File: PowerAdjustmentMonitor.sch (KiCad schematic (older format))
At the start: 0 parts

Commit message: Added Power Control Monitoring Module Schematic
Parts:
- added JP? (x3): JUMPER, ~, symbol JUMPER
- added R? (x8): R, ~, symbol R
- added R? (x2): RVAR, ~, symbol RVAR
- added U? (x2): LM317, ~, symbol LM317
- added U? (x2): 7805, ~, symbol 7805
- added U? (x2): LM324, symbol LM324
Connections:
- new net: R?.1, R?.2, U?.2 (ADJ)
- new net: R?.2, R?.2, U?.2 (ADJ)
- new net +12V: JP?.1, U?.1 (IN), U?.4 (V+), U?.4 (V+), U?.VI
- new net -12V: JP?.1, U?.1 (IN), U?.11 (V-), U?.11 (V-), U?.VI
- new net AGND: JP?.1
- new net FE_V+: JP?.2, U?.VO
- new net FE_V-: JP?.2, U?.VO
- new net GND: JP?.2, R?.1, R?.1, R?.1, R?.2, U?.GND, U?.GND
- new net V+CURR_MON: U?.1, U?.2 (-)
- new net V+_ADJ: R?.2, R?.2
- new net V+_ADJ_MON: R?.1, R?.2
- new net V+_MON: R?.1, R?.1, U?.3 (+), U?.3 (OUT)
- new net V-ADJ_MON: R?.1, R?.2
- new net V-CURR_MON: U?.1, U?.2 (-)
- new net V-_ADJ: R?.1, R?.2
- new net V-_MON: R?.1, R?.2, U?.3 (+), U?.3 (OUT)

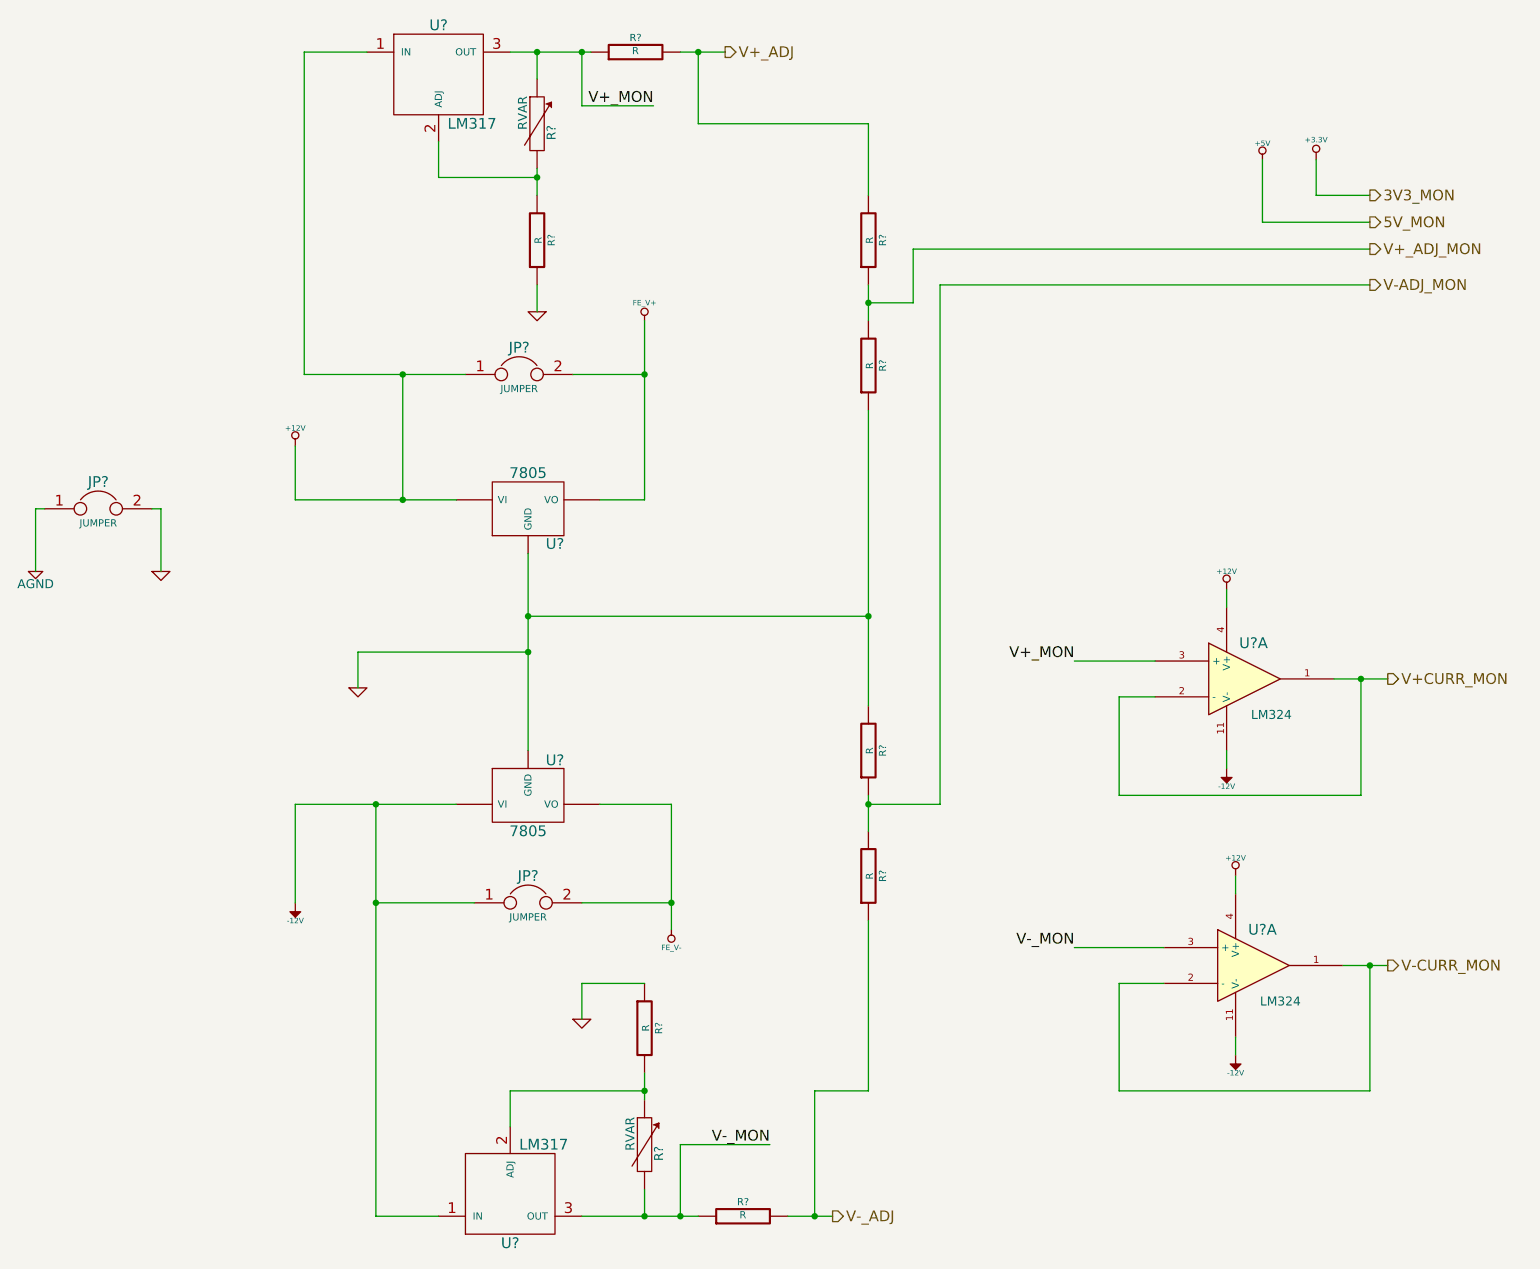
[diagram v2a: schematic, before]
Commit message: Initial Relay PCB Layout
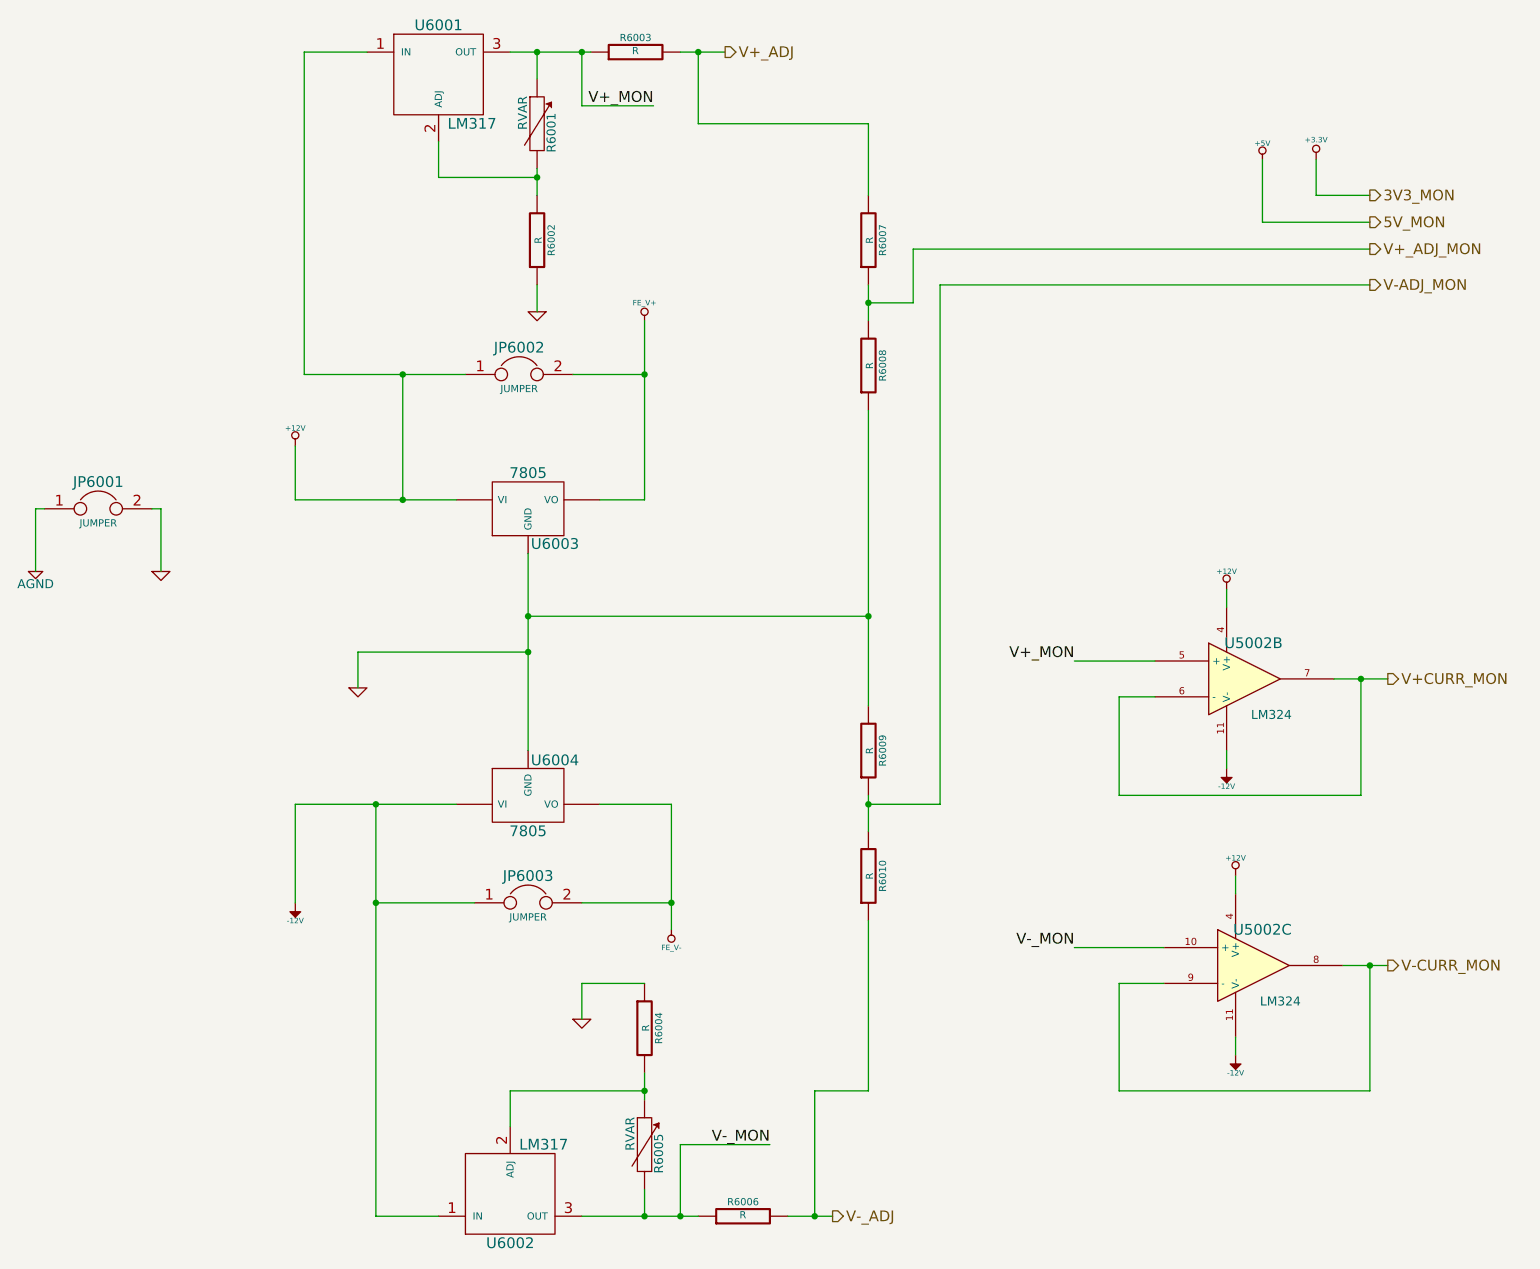
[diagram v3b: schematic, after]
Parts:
- gave numbers to parts that had none: 18
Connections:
- net V+CURR_MON: now also U5002.6 (-), U5002.7; no longer U5002.1, U5002.2 (-)
- net V+_MON: now also U5002.5 (+); no longer U5002.3 (+)
- net V-CURR_MON: now also U5002.8, U5002.9 (-); no longer U5002.1, U5002.2 (-)
- net V-_MON: now also U5002.10 (+); no longer U5002.3 (+)
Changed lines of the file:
@@
 $Descr A4 11693 8268
 encoding utf-8
-Sheet 9 9
+Sheet 6 9
 Title ""
-Date "9 feb 2014"
+Date "17 feb 2014"
 Rev ""
 Comp ""
@@
 $EndDescr
 $Comp
-L +3.3V #PWR?
+L +3.3V #PWR6015
 U 1 1 52F258C0
 P 9300 1600
-F 0 "#PWR?" H 9300 1560 30  0001 C CNN
+F 0 "#PWR6015" H 9300 1560 30  0001 C CNN
 F 1 "+3.3V" H 9300 1710 30  0000 C CNN
 F 2 "" H 9300 1600 60  0000 C CNN
@@
 $EndComp
 $Comp
-L +5V #PWR?
+L +5V #PWR6014
 U 1 1 52F258C6
 P 9000 1600
-F 0 "#PWR?" H 9000 1690 20  0001 C CNN
+F 0 "#PWR6014" H 9000 1690 20  0001 C CNN
 F 1 "+5V" H 9000 1690 30  0000 C CNN
 F 2 "" H 9000 1600 60  0000 C CNN
@@
 $EndComp
 $Comp
-L GND #PWR?
+L GND #PWR6005
 U 1 1 52F2592B
 P 3950 4550
-F 0 "#PWR?" H 3950 4550 30  0001 C CNN
+F 0 "#PWR6005" H 3950 4550 30  0001 C CNN
 F 1 "GND" H 3950 4480 30  0001 C CNN
 F 2 "" H 3950 4550 60  0000 C CNN
@@
 $EndComp
 $Comp
-L -12V #PWR?
+L -12V #PWR6004
 U 1 1 52F25955
 P 3600 5750
-F 0 "#PWR?" H 3600 5880 20  0001 C CNN
+F 0 "#PWR6004" H 3600 5880 20  0001 C CNN
 F 1 "-12V" H 3600 5850 30  0000 C CNN
 F 2 "" H 3600 5750 60  0000 C CNN
@@
 $EndComp
 $Comp
-L +12V #PWR?
+L +12V #PWR6003
 U 1 1 52F25965
 P 3600 3200
-F 0 "#PWR?" H 3600 3150 20  0001 C CNN
+F 0 "#PWR6003" H 3600 3150 20  0001 C CNN
 F 1 "+12V" H 3600 3300 30  0000 C CNN
 F 2 "" H 3600 3200 60  0000 C CNN
@@
 $EndComp
 $Comp
-L LM317 U?
+L LM317 U6002
 U 1 1 52F25974
 P 4800 7350
-F 0 "U?" H 4800 7650 60  0000 C CNN
+F 0 "U6002" H 4800 7650 60  0000 C CNN
 F 1 "LM317" H 4850 7100 60  0000 L CNN
 F 2 "~" H 4800 7350 60  0000 C CNN
@@
 $EndComp
 $Comp
-L JUMPER JP?
+L JUMPER JP6002
 U 1 1 52F259A2
 P 4850 2800
-F 0 "JP?" H 4850 2950 60  0000 C CNN
+F 0 "JP6002" H 4850 2950 60  0000 C CNN
 F 1 "JUMPER" H 4850 2720 40  0000 C CNN
 F 2 "~" H 4850 2800 60  0000 C CNN
@@
 $EndComp
 $Comp
-L JUMPER JP?
+L JUMPER JP6003
 U 1 1 52F259AF
 P 4900 5750
-F 0 "JP?" H 4900 5900 60  0000 C CNN
+F 0 "JP6003" H 4900 5900 60  0000 C CNN
 F 1 "JUMPER" H 4900 5670 40  0000 C CNN
 F 2 "~" H 4900 5750 60  0000 C CNN
@@
 $EndComp
 $Comp
-L AGND #PWR?
+L AGND #PWR6001
 U 1 1 52F25DEE
 P 2150 3900
-F 0 "#PWR?" H 2150 3900 40  0001 C CNN
+F 0 "#PWR6001" H 2150 3900 40  0001 C CNN
 F 1 "AGND" H 2150 3830 50  0000 C CNN
 F 2 "" H 2150 3900 60  0000 C CNN
@@
 $EndComp
 $Comp
-L JUMPER JP?
+L JUMPER JP6001
 U 1 1 52F25DFB
 P 2500 3550
-F 0 "JP?" H 2500 3700 60  0000 C CNN
+F 0 "JP6001" H 2500 3700 60  0000 C CNN
 F 1 "JUMPER" H 2500 3470 40  0000 C CNN
 F 2 "~" H 2500 3550 60  0000 C CNN
@@
 $EndComp
 $Comp
-L GND #PWR?
+L GND #PWR6002
 U 1 1 52F25E16
 P 2850 3900
-F 0 "#PWR?" H 2850 3900 30  0001 C CNN
+F 0 "#PWR6002" H 2850 3900 30  0001 C CNN
 F 1 "GND" H 2850 3830 30  0001 C CNN
 F 2 "" H 2850 3900 60  0000 C CNN
@@
 $EndComp
 $Comp
-L FE_V+ #PWR?
+L FE_V+ #PWR6008
 U 1 1 52F25E8D
 P 5550 2500
-F 0 "#PWR?" H 5550 2600 30  0001 C CNN
+F 0 "#PWR6008" H 5550 2600 30  0001 C CNN
 F 1 "FE_V+" H 5550 2600 30  0000 C CNN
 F 2 "" H 5550 2500 60  0000 C CNN
@@
 $EndComp
 $Comp
-L FE_V- #PWR?
+L FE_V- #PWR6009
 U 1 1 52F25E9C
 P 5700 5900
-F 0 "#PWR?" H 5700 6000 30  0001 C CNN
+F 0 "#PWR6009" H 5700 6000 30  0001 C CNN
 F 1 "FE_V-" H 5700 6000 30  0000 C CNN
 F 2 "" H 5700 5900 60  0000 C CNN
@@
 $EndComp
 $Comp
-L 7805 U?
+L 7805 U6003
 U 1 1 52F25F16
 P 4900 3550
-F 0 "U?" H 5050 3354 60  0000 C CNN
+F 0 "U6003" H 5050 3354 60  0000 C CNN
 F 1 "7805" H 4900 3750 60  0000 C CNN
 F 2 "~" H 4900 3550 60  0000 C CNN
@@
 $EndComp
 $Comp
-L 7805 U?
+L 7805 U6004
 U 1 1 52F25F23
 P 4900 5150
-F 0 "U?" H 5050 4954 60  0000 C CNN
+F 0 "U6004" H 5050 4954 60  0000 C CNN
 F 1 "7805" H 4900 5350 60  0000 C CNN
 F 2 "~" H 4900 5150 60  0000 C CNN
@@
 $EndComp
 $Comp
-L R R?
+L R R6004
 U 1 1 52F25FD8
 P 5550 6450
-F 0 "R?" V 5630 6450 40  0000 C CNN
+F 0 "R6004" V 5630 6450 40  0000 C CNN
 F 1 "R" V 5557 6451 40  0000 C CNN
 F 2 "~" V 5480 6450 30  0000 C CNN
@@
 $EndComp
 $Comp
-L GND #PWR?
+L GND #PWR6007
 U 1 1 52F26054
 P 5200 6400
-F 0 "#PWR?" H 5200 6400 30  0001 C CNN
+F 0 "#PWR6007" H 5200 6400 30  0001 C CNN
 F 1 "GND" H 5200 6330 30  0001 C CNN
 F 2 "" H 5200 6400 60  0000 C CNN
@@
 $EndComp
 $Comp
-L LM317 U?
+L LM317 U6001
 U 1 1 52F26114
 P 4400 1150
-F 0 "U?" H 4400 1450 60  0000 C CNN
+F 0 "U6001" H 4400 1450 60  0000 C CNN
 F 1 "LM317" H 4450 900 60  0000 L CNN
 F 2 "~" H 4400 1150 60  0000 C CNN
@@
 $EndComp
 $Comp
-L R R?
+L R R6002
 U 1 1 52F26120
 P 4950 2050
-F 0 "R?" V 5030 2050 40  0000 C CNN
+F 0 "R6002" V 5030 2050 40  0000 C CNN
 F 1 "R" V 4957 2051 40  0000 C CNN
 F 2 "~" V 4880 2050 30  0000 C CNN
@@
 $EndComp
 $Comp
-L GND #PWR?
+L GND #PWR6006
 U 1 1 52F2612C
 P 4950 2450
-F 0 "#PWR?" H 4950 2450 30  0001 C CNN
+F 0 "#PWR6006" H 4950 2450 30  0001 C CNN
 F 1 "GND" H 4950 2380 30  0001 C CNN
 F 2 "" H 4950 2450 60  0000 C CNN
@@
 V-CURR_MON
 $Comp
-L R R?
+L R R6007
 U 1 1 52F261D2
 P 6800 2050
-F 0 "R?" V 6880 2050 40  0000 C CNN
+F 0 "R6007" V 6880 2050 40  0000 C CNN
 F 1 "R" V 6807 2051 40  0000 C CNN
 F 2 "~" V 6730 2050 30  0000 C CNN
@@
 $EndComp
 $Comp
-L R R?
+L R R6008
 U 1 1 52F261D8
 P 6800 2750
-F 0 "R?" V 6880 2750 40  0000 C CNN
+F 0 "R6008" V 6880 2750 40  0000 C CNN
 F 1 "R" V 6807 2751 40  0000 C CNN
 F 2 "~" V 6730 2750 30  0000 C CNN
@@
 $EndComp
 $Comp
-L R R?
+L R R6009
 U 1 1 52F261DE
 P 6800 4900
-F 0 "R?" V 6880 4900 40  0000 C CNN
+F 0 "R6009" V 6880 4900 40  0000 C CNN
 F 1 "R" V 6807 4901 40  0000 C CNN
 F 2 "~" V 6730 4900 30  0000 C CNN
@@
 $EndComp
 $Comp
-L R R?
+L R R6010
 U 1 1 52F261E4
 P 6800 5600
-F 0 "R?" V 6880 5600 40  0000 C CNN
+F 0 "R6010" V 6880 5600 40  0000 C CNN
 F 1 "R" V 6807 5601 40  0000 C CNN
 F 2 "~" V 6730 5600 30  0000 C CNN
@@
 	9000 1950 9600 1950
 $Comp
-L R R?
+L R R6006
 U 1 1 52F2653F
 P 6100 7500
-F 0 "R?" V 6180 7500 40  0000 C CNN
+F 0 "R6006" V 6180 7500 40  0000 C CNN
 F 1 "R" V 6107 7501 40  0000 C CNN
 F 2 "~" V 6030 7500 30  0000 C CNN
@@
 	6350 7500 6600 7500
 $Comp
-L R R?
+L R R6003
 U 1 1 52F26669
 P 5500 1000
-F 0 "R?" V 5580 1000 40  0000 C CNN
+F 0 "R6003" V 5580 1000 40  0000 C CNN
 F 1 "R" V 5507 1001 40  0000 C CNN
 F 2 "~" V 5430 1000 30  0000 C CNN
@@
 Connection ~ 4950 1000
 $Comp
-L LM324 U?
-U 1 1 52F26EAF
+L LM324 U5002
+U 3 1 52F26EAF
 P 8950 6100
-F 0 "U?" H 9000 6300 60  0000 C CNN
+F 0 "U5002" H 9000 6300 60  0000 C CNN
 F 1 "LM324" H 9100 5900 50  0000 C CNN
 F 2 "" H 8950 6100 60  0000 C CNN
 F 3 "" H 8950 6100 60  0000 C CNN
-	1    8950 6100
-	1    0    0    -1
-$EndComp
-$Comp
-L -12V #PWR?
+	3    8950 6100
+	1    0    0    -1
+$EndComp
+$Comp
+L -12V #PWR6013
 U 1 1 52F26EBC
 P 8850 6600
-F 0 "#PWR?" H 8850 6730 20  0001 C CNN
+F 0 "#PWR6013" H 8850 6730 20  0001 C CNN
 F 1 "-12V" H 8850 6700 30  0000 C CNN
 F 2 "" H 8850 6600 60  0000 C CNN
@@
 $EndComp
 $Comp
-L +12V #PWR?
+L +12V #PWR6012
 U 1 1 52F26EC2
 P 8850 5600
-F 0 "#PWR?" H 8850 5550 20  0001 C CNN
+F 0 "#PWR6012" H 8850 5550 20  0001 C CNN
 F 1 "+12V" H 8850 5700 30  0000 C CNN
 F 2 "" H 8850 5600 60  0000 C CNN
@@
 	8850 6600 8850 6500
 $Comp
-L LM324 U?
-U 1 1 52F27003
+L LM324 U5002
+U 2 1 52F27003
 P 8900 4500
-F 0 "U?" H 8950 4700 60  0000 C CNN
+F 0 "U5002" H 8950 4700 60  0000 C CNN
 F 1 "LM324" H 9050 4300 50  0000 C CNN
 F 2 "" H 8900 4500 60  0000 C CNN
 F 3 "" H 8900 4500 60  0000 C CNN
-	1    8900 4500
-	1    0    0    -1
-$EndComp
-$Comp
-L -12V #PWR?
+	2    8900 4500
+	1    0    0    -1
+$EndComp
+$Comp
+L -12V #PWR6011
 U 1 1 52F27009
 P 8800 5000
-F 0 "#PWR?" H 8800 5130 20  0001 C CNN
+F 0 "#PWR6011" H 8800 5130 20  0001 C CNN
 F 1 "-12V" H 8800 5100 30  0000 C CNN
 F 2 "" H 8800 5000 60  0000 C CNN
@@
 $EndComp
 $Comp
-L +12V #PWR?
+L +12V #PWR6010
 U 1 1 52F2700F
 P 8800 4000
-F 0 "#PWR?" H 8800 3950 20  0001 C CNN
+F 0 "#PWR6010" H 8800 3950 20  0001 C CNN
 F 1 "+12V" H 8800 4100 30  0000 C CNN
 F 2 "" H 8800 4000 60  0000 C CNN
@@
 V-_MON
 $Comp
-L RVAR R?
+L RVAR R6005
 U 1 1 52F275AF
 P 5550 7100
-F 0 "R?" V 5630 7050 50  0000 C CNN
+F 0 "R6005" V 5630 7050 50  0000 C CNN
 F 1 "RVAR" V 5470 7160 50  0000 C CNN
 F 2 "~" H 5550 7100 60  0000 C CNN
@@
 $EndComp
 $Comp
-L RVAR R?
+L RVAR R6001
 U 1 1 52F275BE
 P 4950 1400
-F 0 "R?" V 5030 1350 50  0000 C CNN
+F 0 "R6001" V 5030 1350 50  0000 C CNN
 F 1 "RVAR" V 4870 1460 50  0000 C CNN
 F 2 "~" H 4950 1400 60  0000 C CNN
